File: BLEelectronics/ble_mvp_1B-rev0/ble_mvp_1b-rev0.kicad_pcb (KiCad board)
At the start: 2 copper layers, 36 x 28.3 mm, 71 parts, among them IC1 LTC4412xS6, IC2 LTC4054LES5-4.2#TRPBF, IC3 PCF8523T, IC4 MX25R6435FM2IL0, J1 USB_B_Micro, J3 Conn_02x05_Odd_Even, Q1 Si2307CDS, SW1 NO, SW2 SW_MEC_5G, U1 BAT-HLD-001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

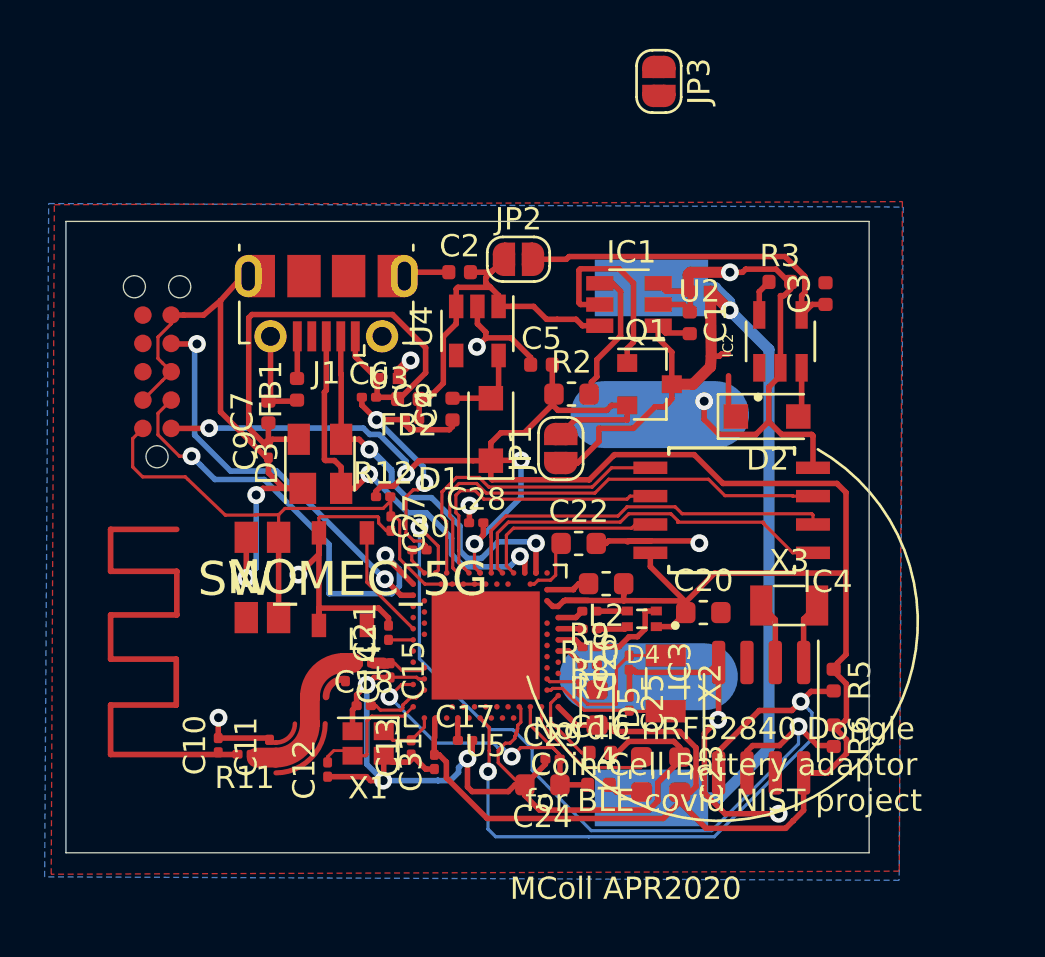
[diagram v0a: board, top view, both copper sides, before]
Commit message: increased track widths on long traces on mvp1b-rev0
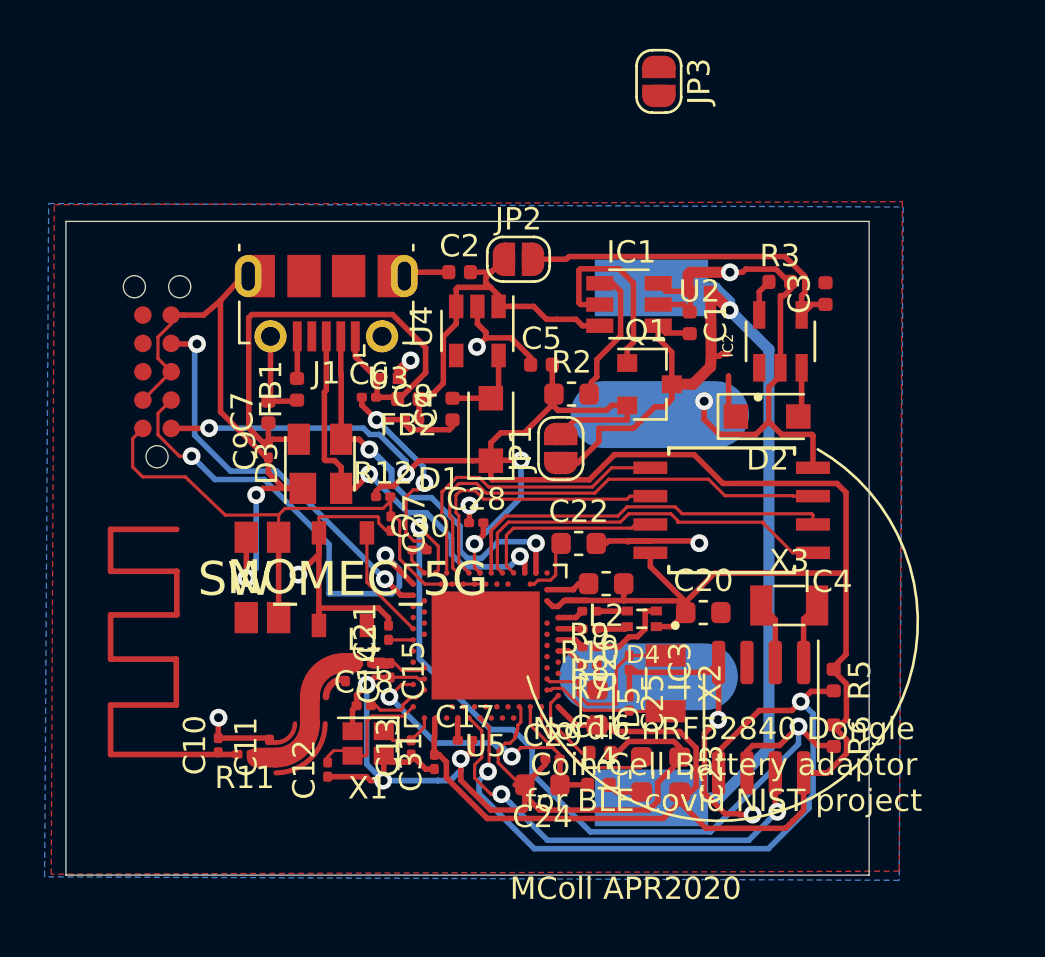
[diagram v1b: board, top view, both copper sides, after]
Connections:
- net /CS renamed /~CS~
- net /SIO3 renamed /flash~RESET~
- IC3 pad 7: Net-(IC3-Pad7) -> /~INT1~
- IC4 pad 3: /WP -> /~WP~
- U5 pad A16: Net-(U5-PadA16) -> /~INT1~
- U5 pad AD18: /WP -> /~WP
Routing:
- net /~INT1~: track 0.00 -> 20.1 mm, vias 0 -> 2
- net /SDA: track 30.9 -> 32.8 mm
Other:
- board size 36 x 28.3 mm -> 36 x 29.3 mm
